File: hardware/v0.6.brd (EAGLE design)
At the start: 56.8 x 32.4 mm, 31 parts, among them J2 MAGJACK, U1 ATMEGA168P, U2 ENC28J60, Y1 CRYSTAL-GROUNDED

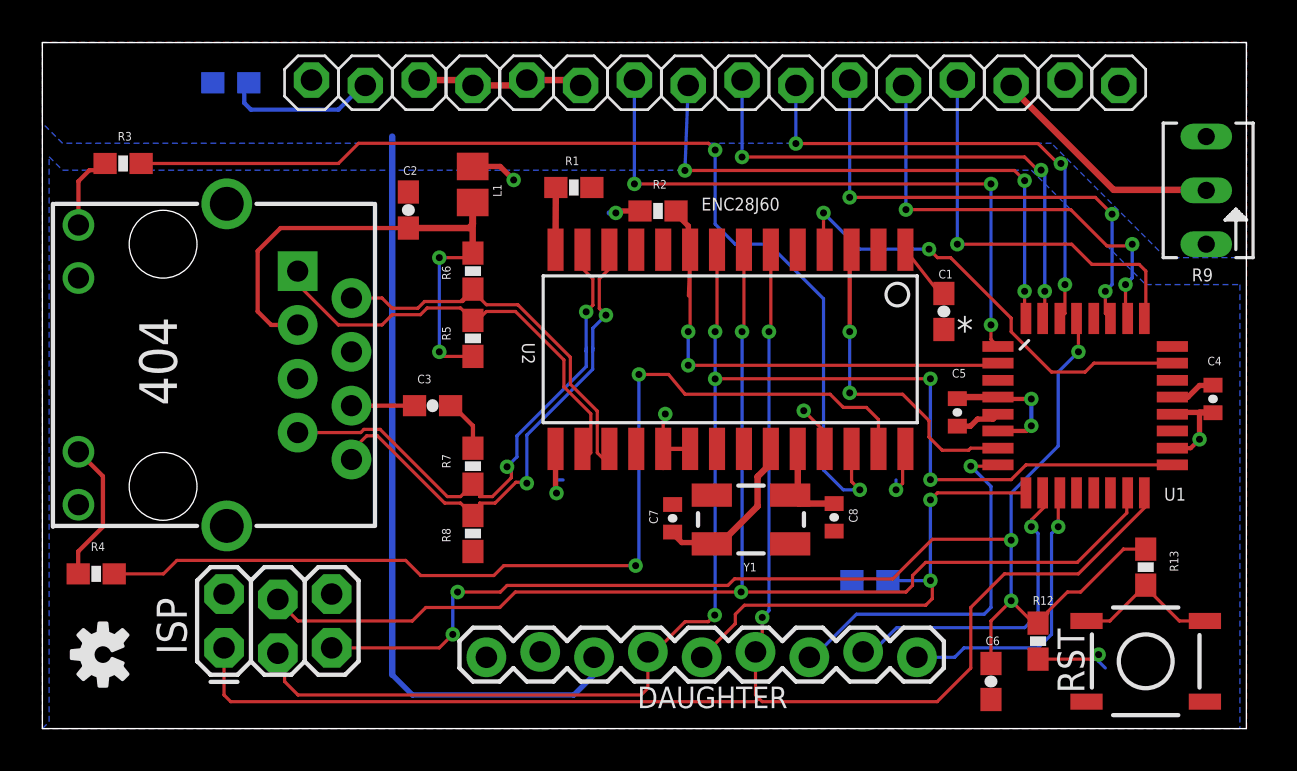
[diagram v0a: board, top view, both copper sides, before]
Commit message: Fixed tx diff pair impedence matching (hardware)
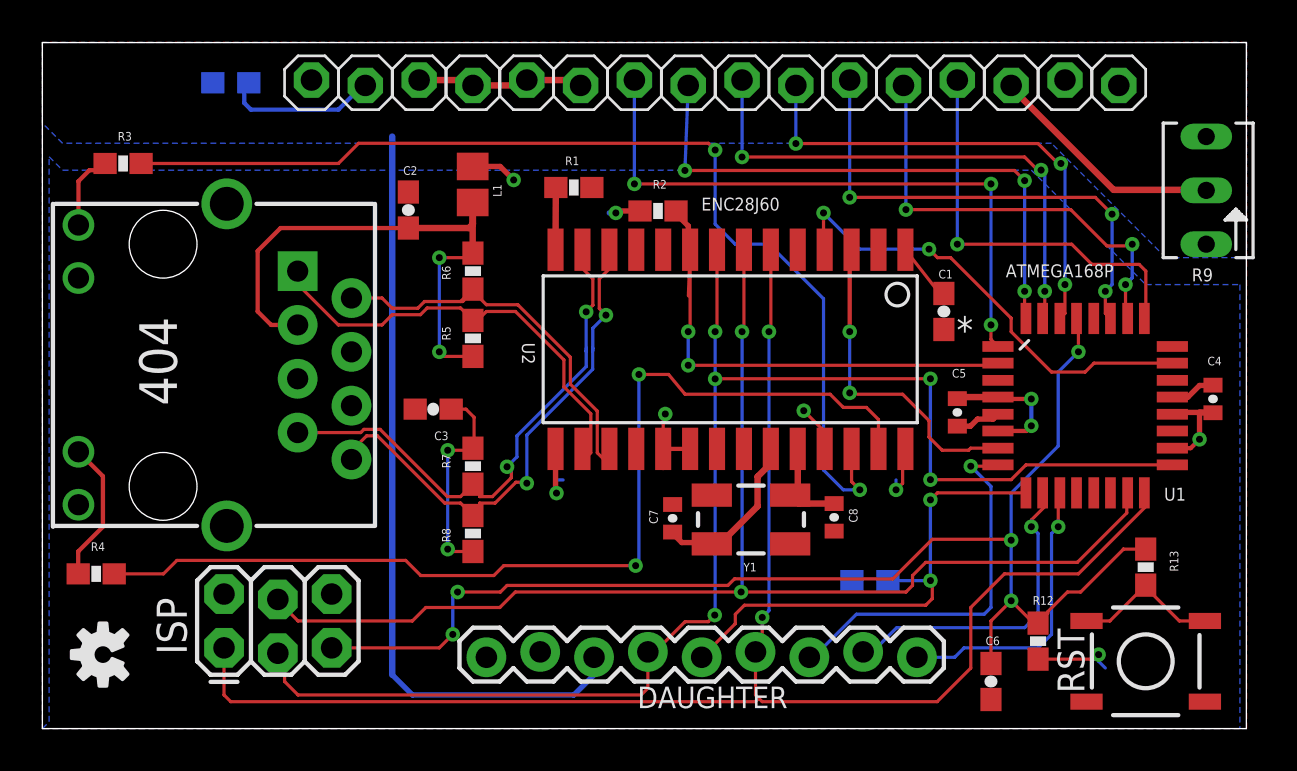
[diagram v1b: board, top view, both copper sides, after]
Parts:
- moved C3 0.17 mm to (18.8, 19.5), turned to 0 degrees
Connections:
- removed net N$5: C3.2, J2.6
- new net TDCAP: C3.2, R7.2, R8.2
- net GND: no longer R7.2, R8.2
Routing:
- net TDCAP: track 0.00 -> 9.94 mm, vias 0 -> 2
- net N$5: track 2.98 -> 0.00 mm
- net GND: track 14.7 -> 12.2 mm
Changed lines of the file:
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@@
 <attribute name="OC_FARNELL" value="1636932" x="49.53" y="19.685" size="1.778" layer="27" display="off"/>
 <attribute name="NAME" x="53.2511" y="15.2019" size="0.6096" layer="25" ratio="10" rot="SR0"/>
-<attribute name="VALUE" x="45.7835" y="25.7429" size="0.6096" layer="27" ratio="7" rot="SR0"/>
+<attribute name="VALUE" x="45.7835" y="25.7429" size="0.6096" layer="25" ratio="7" rot="SR0"/>
 </element>
 <element name="ISP" library="SparkFun-Connectors" package="2X3_LOCK" value="AVR_SPI_PRG_62X3_LOCK" x="8.89" y="8.255" smashed="yes">
@@
 <attribute name="VALUE" x="16.7386" y="26.6065" size="0.4064" layer="27" font="vector"/>
 </element>
-<element name="C3" library="SparkFun-Passives" package="0603-CAP" value="0.01uF" x="18.7325" y="19.685" smashed="yes" rot="R180">
-<attribute name="NAME" x="18.6817" y="21.1455" size="0.4064" layer="25" rot="R180"/>
-<attribute name="VALUE" x="19.7485" y="18.923" size="0.4064" layer="27" font="vector" rot="R180"/>
+<element name="C3" library="SparkFun-Passives" package="0603-CAP" value="0.01uF" x="18.761075" y="19.5199" smashed="yes">
+<attribute name="NAME" x="18.811875" y="18.0594" size="0.4064" layer="25"/>
+<attribute name="VALUE" x="17.745075" y="20.2819" size="0.4064" layer="27" font="vector"/>
 </element>
 <element name="R7" library="SparkFun-Passives" package="0603-RES" value="50" x="20.6375" y="16.8275" smashed="yes" rot="R90">
@@
 <contactref element="J2" pad="10"/>
 <contactref element="C2" pad="1"/>
-<contactref element="C3" pad="1"/>
-<contactref element="R7" pad="2"/>
-<contactref element="R8" pad="2"/>
 <contactref element="J2" pad="M1"/>
 <contactref element="J2" pad="M2"/>
 <contactref element="R9" pad="A"/>
-<wire x1="19.5825" y1="19.685" x2="19.685" y2="19.685" width="0.2032" layer="1"/>
-<wire x1="19.685" y1="19.685" x2="20.6375" y2="18.7325" width="0.2032" layer="1"/>
-<wire x1="20.6375" y1="18.7325" x2="20.6375" y2="17.6775" width="0.2032" layer="1"/>
 <wire x1="18.0975" y1="35.052" x2="20.3835" y2="35.052" width="0.3048" layer="1"/>
 <wire x1="20.3835" y1="35.052" x2="20.6375" y2="34.798" width="0.3048" layer="1"/>
@@
 <contactref element="Y1" pad="2"/>
 <contactref element="Y1" pad="4"/>
+<contactref element="C3" pad="1"/>
 </signal>
 <signal name="+5V">
@@
 <wire x1="25.981025" y1="22.2504" x2="25.9842" y2="22.247225" width="0.1524" layer="16"/>
 </signal>
-<signal name="N$5">
-<contactref element="C3" pad="2"/>
-<contactref element="J2" pad="6"/>
-<wire x1="14.905" y1="19.685" x2="17.8825" y2="19.685" width="0.2032" layer="1"/>
-</signal>
 <signal name="PHY_RD_P">
 <contactref element="R5" pad="1"/>
@@
 <wire x1="31.909125" y1="13.16355" x2="31.909775" y2="13.1629" width="0.3048" layer="1"/>
 </signal>
+<signal name="TDCAP">
+<contactref element="R7" pad="2"/>
+<contactref element="R8" pad="2"/>
+<contactref element="C3" pad="2"/>
+<wire x1="19.611075" y1="19.5199" x2="20.3073" y2="19.5199" width="0.1524" layer="1"/>
+<wire x1="20.3073" y1="19.5199" x2="20.691475" y2="19.135725" width="0.1524" layer="1"/>
+<wire x1="20.691475" y1="19.135725" x2="20.691475" y2="17.731475" width="0.1524" layer="1"/>
+<wire x1="20.691475" y1="17.731475" x2="20.6375" y2="17.6775" width="0.1524" layer="1"/>
+<wire x1="20.57945" y1="17.73555" x2="20.6375" y2="17.6775" width="0.1524" layer="1"/>
+<wire x1="20.6375" y1="12.8025" x2="19.5571" y2="12.8025" width="0.1524" layer="1"/>
+<wire x1="19.5571" y1="12.8025" x2="19.446875" y2="12.912725" width="0.1524" layer="1"/>
+<via x="19.446875" y="12.912725" extent="1-16" drill="0.3302" diameter="0.3048" shape="octagon"/>
+<wire x1="19.446875" y1="12.912725" x2="19.446875" y2="17.579975" width="0.1524" layer="16"/>
+<via x="19.446875" y="17.579975" extent="1-16" drill="0.3302" diameter="0.3048" shape="octagon"/>
+<wire x1="19.446875" y1="17.579975" x2="20.539975" y2="17.579975" width="0.1524" layer="1"/>
+<wire x1="20.539975" y1="17.579975" x2="20.6375" y2="17.6775" width="0.1524" layer="1"/>
+</signal>
 </signals>

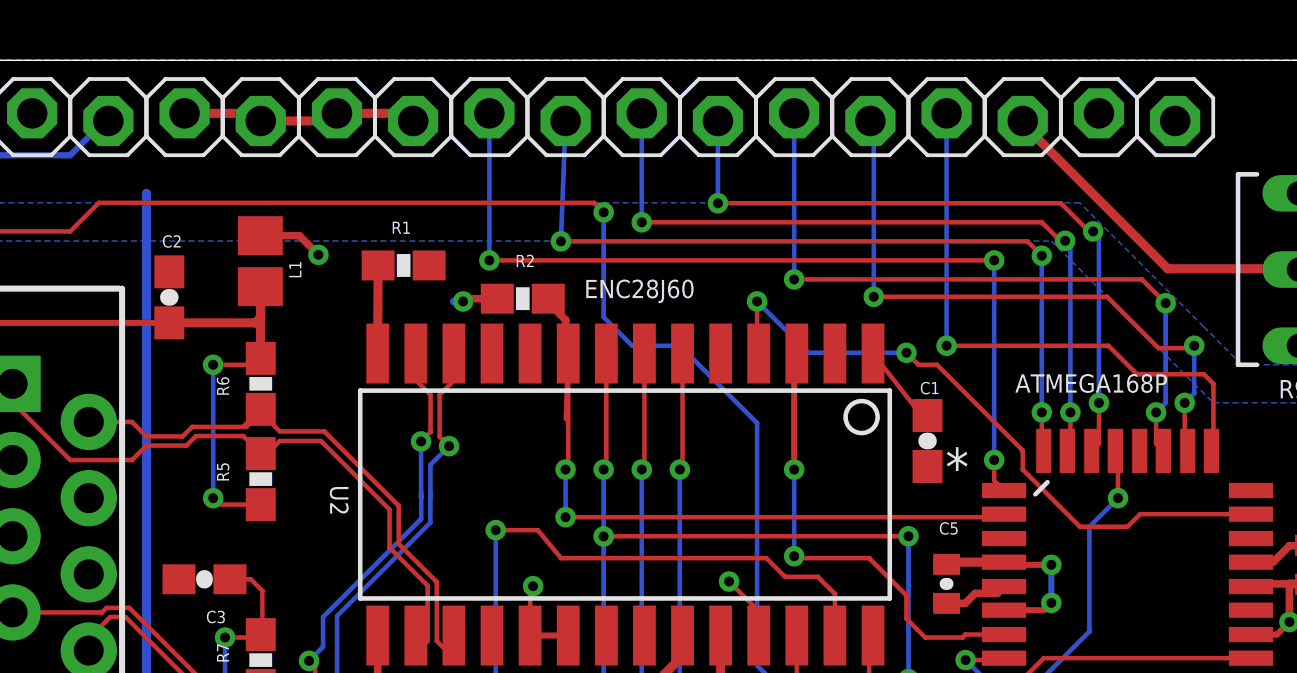
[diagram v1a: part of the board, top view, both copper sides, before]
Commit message: routed correct (upper) 4 bit lcd bus (hardware)
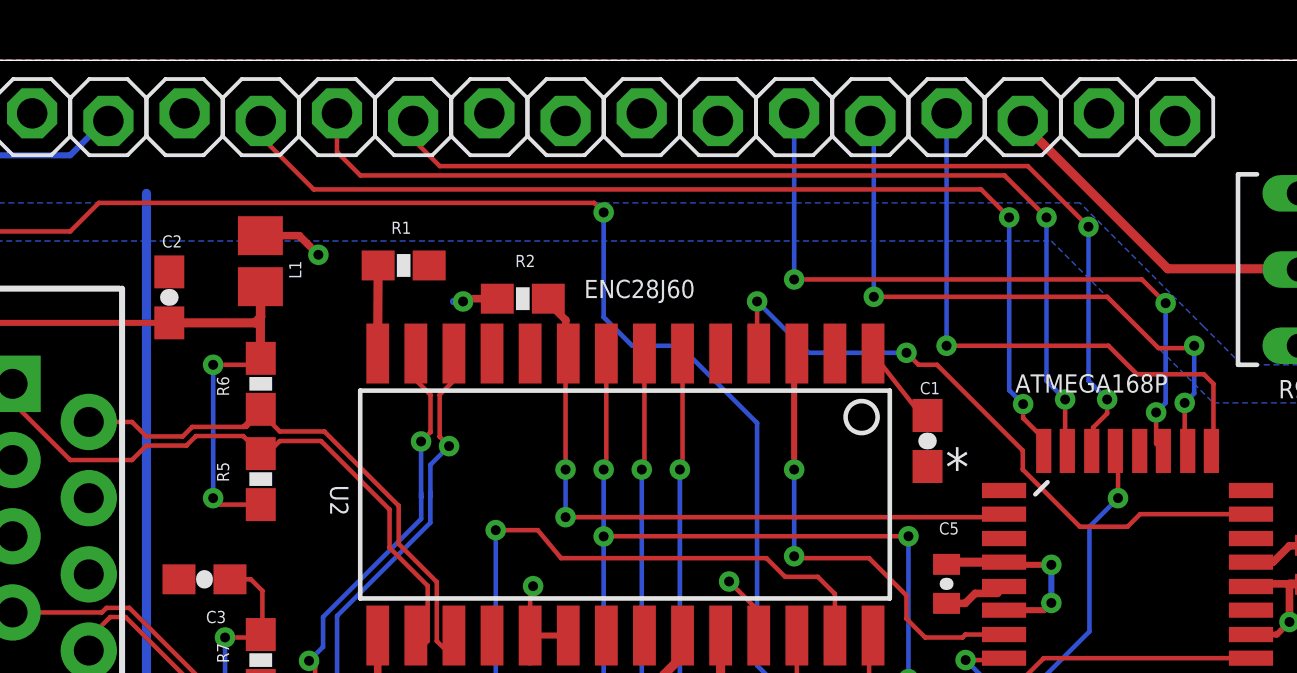
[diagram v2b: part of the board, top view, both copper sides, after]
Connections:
- removed net LCD_D0: LCD1.7, U1.30
- removed net LCD_D1: LCD1.8, U1.31
- removed net LCD_D2: LCD1.9, U1.32
- removed net LCD_D3: LCD1.10, U1.1
- new net LCD_D4: LCD1.11, U1.30
- new net LCD_D5: LCD1.12, U1.31
- new net LCD_D6: LCD1.13, U1.32
- new net LCD_D7: LCD1.14, U1.1
- net GND: now also LCD1.10, LCD1.7, LCD1.8, LCD1.9; no longer LCD1.11, LCD1.12, LCD1.13, LCD1.14
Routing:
- net LCD_D6: track 0.00 -> 34.8 mm, vias 0 -> 2
- net LCD_D5: track 0.00 -> 33.9 mm, vias 0 -> 2
- net LCD_D4: track 0.00 -> 32.3 mm, vias 0 -> 2
- net LCD_D3: track 29.5 -> 0.00 mm, vias 3 -> 0
- net LCD_D2: track 26.8 -> 0.00 mm, vias 3 -> 0
- net LCD_D1: track 25.1 -> 0.00 mm, vias 3 -> 0
- net LCD_D0: track 23.1 -> 0.00 mm, vias 3 -> 0
- net GND: track 12.2 -> 4.30 mm
- net PHY_CS: track 24.4 -> 22.3 mm

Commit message: fixed last commit (hardware)
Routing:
- net LCD_D7: track 0.00 -> 39.0 mm, vias 0 -> 3
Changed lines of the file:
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@@
 <wire x1="4.9775" y1="31.115" x2="14.2875" y2="31.115" width="0.1524" layer="1"/>
 <wire x1="14.2875" y1="31.115" x2="15.24" y2="32.0675" width="0.1524" layer="1"/>
-<wire x1="15.24" y1="32.0675" x2="31.75" y2="32.0675" width="0.1524" layer="1"/>
-<wire x1="31.75" y1="32.0675" x2="32.0675" y2="31.75" width="0.1524" layer="1"/>
 <via x="32.0675" y="31.75" extent="1-16" drill="0.3302" shape="octagon"/>
 <wire x1="32.0675" y1="31.75" x2="32.0675" y2="28.2575" width="0.1524" layer="16"/>
@@
 <wire x1="38.89375" y1="15.713075" x2="38.115875" y2="15.713075" width="0.1524" layer="16"/>
 <wire x1="38.115875" y1="15.713075" x2="37.182425" y2="16.646525" width="0.1524" layer="16"/>
+<wire x1="15.24" y1="32.0675" x2="15.2654" y2="32.0675" width="0.1524" layer="1"/>
+<wire x1="15.2654" y1="32.0675" x2="15.86865" y2="32.67075" width="0.1524" layer="1"/>
+<wire x1="15.86865" y1="32.67075" x2="21.936075" y2="32.67075" width="0.1524" layer="1"/>
+<wire x1="21.936075" y1="32.67075" x2="22.71395" y2="31.892875" width="0.1524" layer="1"/>
+<wire x1="22.71395" y1="31.892875" x2="31.924625" y2="31.892875" width="0.1524" layer="1"/>
+<wire x1="31.924625" y1="31.892875" x2="32.0675" y2="31.75" width="0.1524" layer="1"/>
 </signal>
 <signal name="PHY_TD_N">
@@
 <contactref element="U1" pad="32"/>
 <contactref element="LCD1" pad="13"/>
-<wire x1="20.6375" y1="34.798" x2="20.6375" y2="34.280475" width="0.1524" layer="1"/>
-<wire x1="20.6375" y1="34.280475" x2="22.4028" y2="32.515175" width="0.1524" layer="1"/>
-<wire x1="22.4028" y1="32.515175" x2="44.650025" y2="32.515175" width="0.1524" layer="1"/>
 <wire x1="44.650025" y1="32.515175" x2="45.583475" y2="31.581725" width="0.1524" layer="1"/>
 <via x="45.583475" y="31.581725" extent="1-16" drill="0.3302" diameter="0.3048" shape="octagon"/>
@@
 <wire x1="46.0502" y1="24.892" x2="46.736" y2="24.2062" width="0.1524" layer="1"/>
 <wire x1="46.736" y1="23.7998" x2="46.736" y2="24.2062" width="0.1524" layer="1"/>
+<wire x1="21.415375" y1="34.280475" x2="23.180675" y2="32.515175" width="0.1524" layer="1"/>
+<wire x1="23.180675" y1="32.515175" x2="44.650025" y2="32.515175" width="0.1524" layer="1"/>
+<wire x1="21.415375" y1="34.280475" x2="21.155025" y2="34.280475" width="0.1524" layer="1"/>
+<wire x1="21.155025" y1="34.280475" x2="20.6375" y2="34.798" width="0.1524" layer="1"/>
 </signal>
 <signal name="LCD_D7">
 <contactref element="U1" pad="1"/>
 <contactref element="LCD1" pad="14"/>
-<wire x1="18.0975" y1="35.052" x2="45.4152" y2="22.479" width="0" layer="19" extent="1-1"/>
+<wire x1="45.4152" y1="22.479" x2="45.4152" y2="23.0378" width="0.1524" layer="1"/>
+<wire x1="45.4152" y1="23.0378" x2="44.961175" y2="23.491825" width="0.1524" layer="1"/>
+<via x="44.961175" y="23.491825" extent="1-16" drill="0.3302" diameter="0.3048" shape="octagon"/>
+<wire x1="44.961175" y1="23.491825" x2="44.961175" y2="30.025975" width="0.1524" layer="16"/>
+<wire x1="44.961175" y1="30.025975" x2="44.650025" y2="30.337125" width="0.1524" layer="16"/>
+<via x="44.650025" y="30.337125" extent="1-16" drill="0.3302" diameter="0.3048" shape="octagon"/>
+<wire x1="44.650025" y1="30.337125" x2="28.781375" y2="30.337125" width="0.1524" layer="1"/>
+<wire x1="28.781375" y1="30.337125" x2="27.847925" y2="31.270575" width="0.1524" layer="1"/>
+<wire x1="27.847925" y1="31.270575" x2="22.247225" y2="31.270575" width="0.1524" layer="1"/>
+<wire x1="22.247225" y1="31.270575" x2="21.46935" y2="32.04845" width="0.1524" layer="1"/>
+<wire x1="21.46935" y1="32.04845" x2="18.0467" y2="32.04845" width="0.1524" layer="1"/>
+<wire x1="18.0467" y1="32.04845" x2="17.891125" y2="31.892875" width="0.1524" layer="1"/>
+<via x="17.891125" y="31.892875" extent="1-16" drill="0.3302" diameter="0.3048" shape="octagon"/>
+<wire x1="17.891125" y1="31.892875" x2="17.891125" y2="34.845625" width="0.1524" layer="16"/>
+<wire x1="17.891125" y1="34.845625" x2="18.0975" y2="35.052" width="0.1524" layer="16"/>
 </signal>
 </signals>
